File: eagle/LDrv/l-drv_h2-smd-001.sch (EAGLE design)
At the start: 26 parts, among them IC2 74AC132D, IC3 74AC132D, IC4 74AC132D

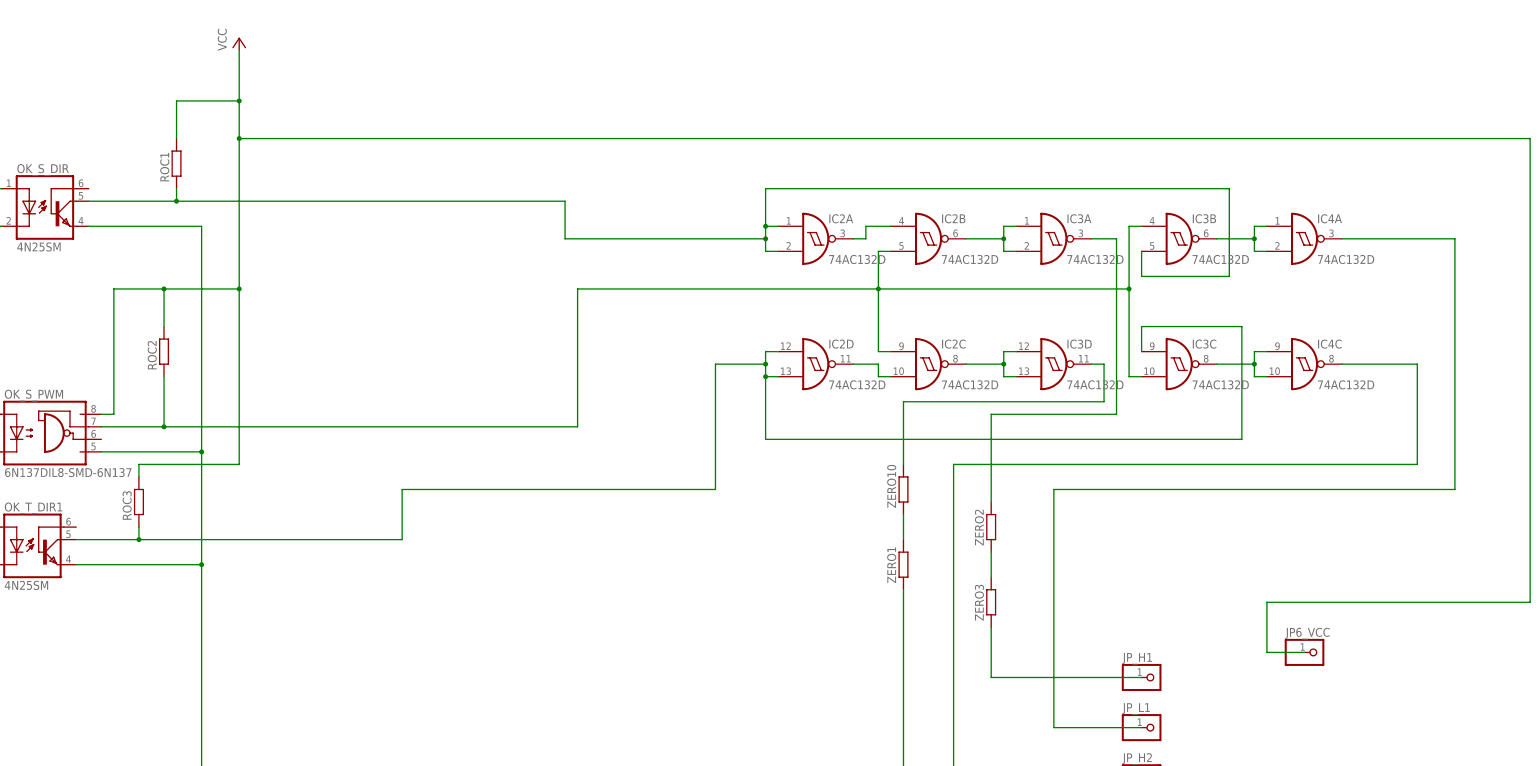
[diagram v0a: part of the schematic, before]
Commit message: SMD logic circit
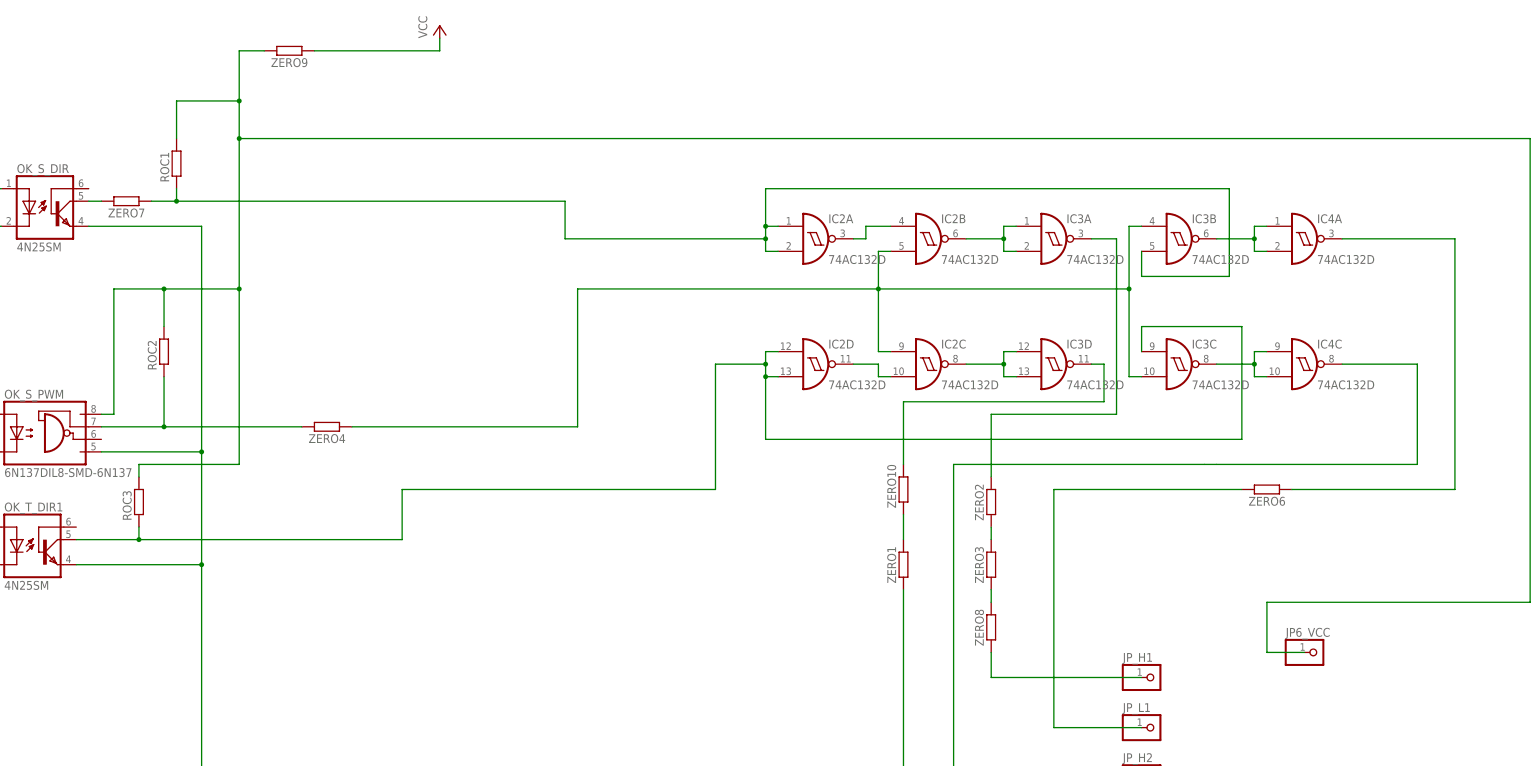
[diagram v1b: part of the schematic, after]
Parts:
- added ZERO4, ZERO6, ZERO7, ZERO8, ZERO9: (no value), rcl:R-EU_R1206
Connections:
- new net N$20: OK_S_PWM.VE, ROC2.1, ZERO4.2
- new net N$23: JP_L1.1, ZERO6.2
- new net N$24: OK_S_DIR.COL, ZERO7.2
- new net N$25: ZERO3.1, ZERO8.2
- new net N$26: JP6_VCC.1, OK_S_PWM.VCC, ROC1.2, ROC2.2, ROC3.2, ZERO9.2
- net N$14: now also ZERO8.1; no longer ZERO3.1
- net N$17: now also ZERO6.1; no longer JP_L1.1
- net N$D1: now also ZERO7.1; no longer OK_S_DIR.COL
- net N$PWM: now also ZERO4.1; no longer OK_S_PWM.VE, ROC2.1
- net VCC: now also ZERO9.1; no longer JP6_VCC.1, OK_S_PWM.VCC, ROC1.2, ROC2.2, ROC3.2
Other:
- moved on the sheet: ZERO2, ZERO3

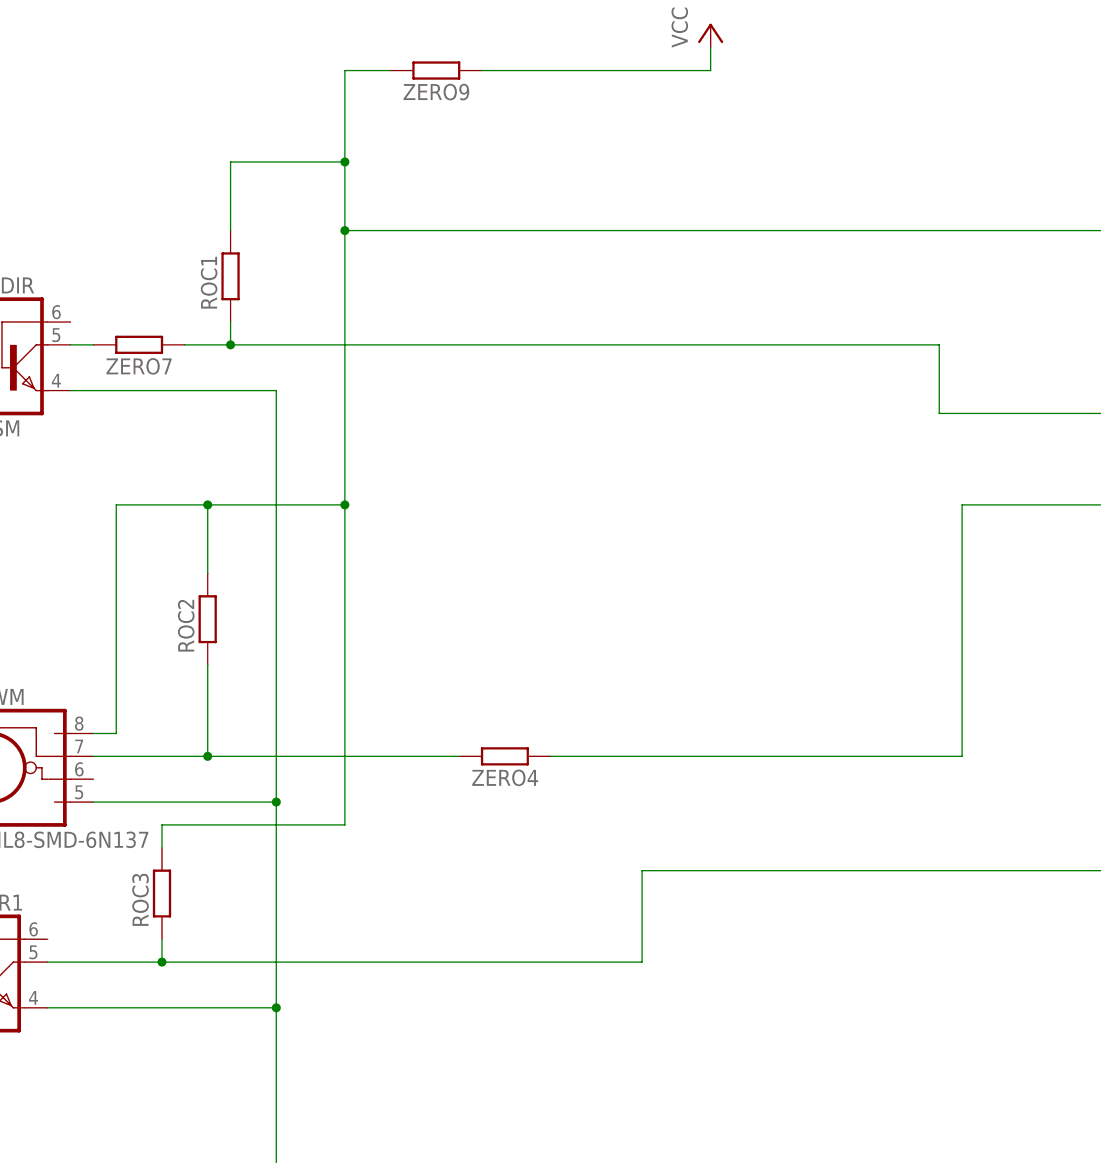
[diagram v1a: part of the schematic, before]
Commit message: SMD for logic drv
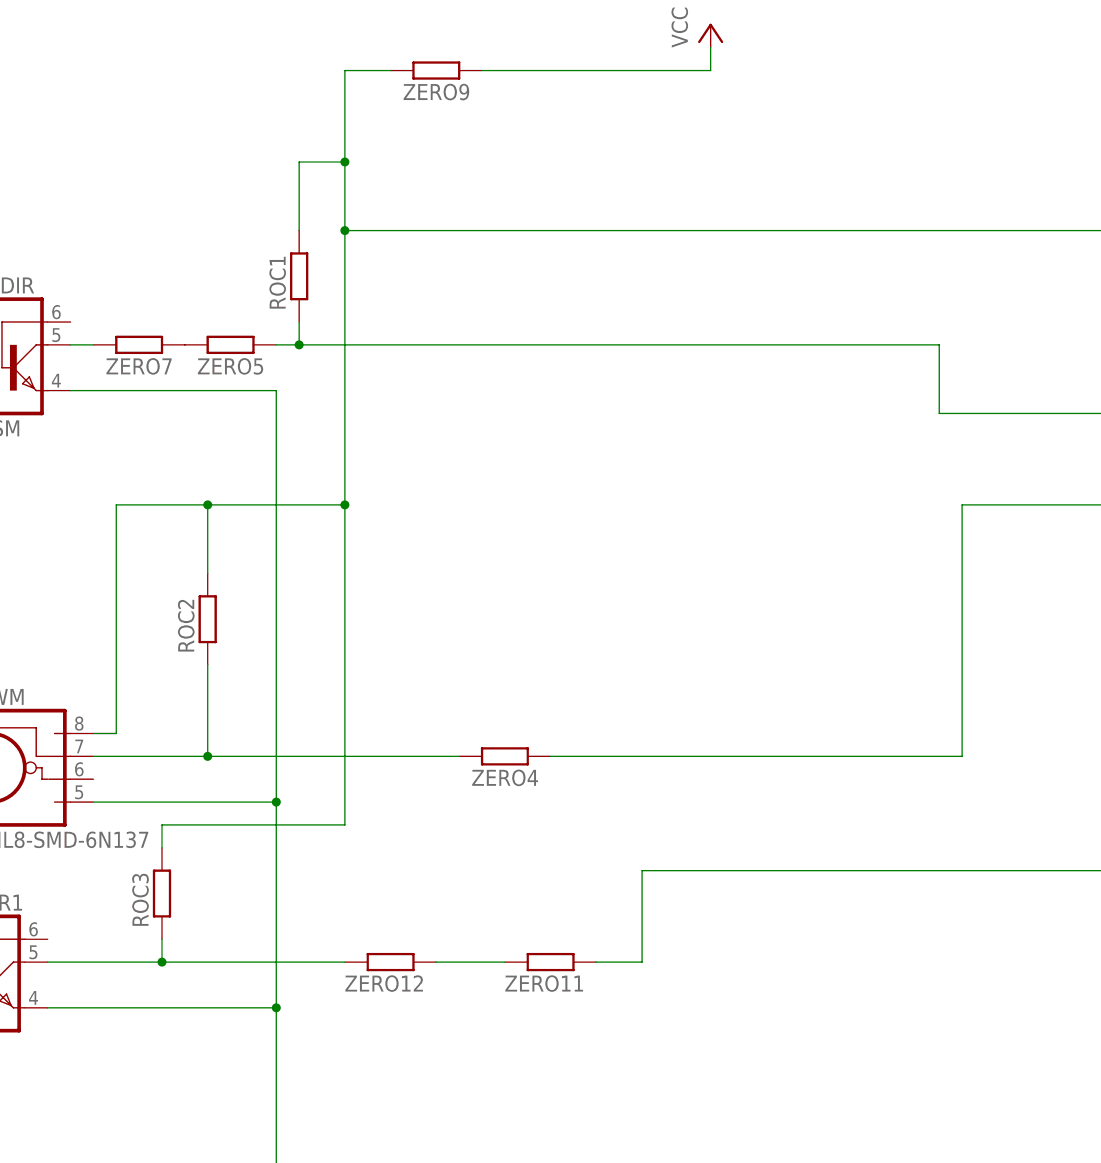
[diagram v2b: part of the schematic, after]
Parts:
- added ZERO11, ZERO12, ZERO5: (no value), rcl:R-EU_R1206
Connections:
- new net N$22: ZERO5.2, ZERO7.1
- new net N$27: OK_T_DIR1.COL, ROC3.1, ZERO12.2
- new net N$28: ZERO11.2, ZERO12.1
- net N$D1: now also ZERO5.1; no longer ZERO7.1
- net N$D2: now also ZERO11.1; no longer OK_T_DIR1.COL, ROC3.1
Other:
- moved on the sheet: ROC1
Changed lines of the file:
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@@
 <setting verticaltext="up"/>
 </settings>
-<grid distance="0.1" unitdist="inch" unit="inch" style="lines" multiple="1" display="yes" altdistance="0.01" altunitdist="inch" altunit="inch"/>
+<grid distance="0.1" unitdist="inch" unit="inch" style="lines" multiple="1" display="no" altdistance="0.01" altunitdist="inch" altunit="inch"/>
 <layers>
 <layer number="1" name="Top" color="4" fill="1" visible="no" active="no"/>
@@
 <part name="ZERO8" library="rcl" deviceset="R-EU_" device="R1206"/>
 <part name="ZERO9" library="rcl" deviceset="R-EU_" device="R1206"/>
+<part name="ZERO5" library="rcl" deviceset="R-EU_" device="R1206"/>
+<part name="ZERO11" library="rcl" deviceset="R-EU_" device="R1206"/>
+<part name="ZERO12" library="rcl" deviceset="R-EU_" device="R1206"/>
 </parts>
 <sheets>
@@
 <instance part="GND1" gate="1" x="83.82" y="-111.76"/>
 <instance part="P+1" gate="VCC" x="132.08" y="93.98"/>
-<instance part="ROC1" gate="G$1" x="78.74" y="66.04" rot="R90"/>
+<instance part="ROC1" gate="G$1" x="86.36" y="66.04" rot="R90"/>
 <instance part="ROC2" gate="G$1" x="76.2" y="27.94" rot="R90"/>
 <instance part="ROC3" gate="G$1" x="71.12" y="-2.54" rot="R90"/>
@@
 <instance part="ZERO8" gate="G$1" x="243.84" y="-27.94" rot="R90"/>
 <instance part="ZERO9" gate="G$1" x="101.6" y="88.9" rot="R180"/>
+<instance part="ZERO5" gate="G$1" x="78.74" y="58.42" rot="R180"/>
+<instance part="ZERO11" gate="G$1" x="114.3" y="-10.16" rot="R180"/>
+<instance part="ZERO12" gate="G$1" x="96.52" y="-10.16" rot="R180"/>
 </instances>
 <busses>
@@
 <net name="N$D2" class="0">
 <segment>
-<pinref part="OK_T_DIR1" gate="G$1" pin="COL"/>
-<wire x1="58.42" y1="-10.16" x2="71.12" y2="-10.16" width="0.1524" layer="91"/>
-<pinref part="ROC3" gate="G$1" pin="1"/>
-<wire x1="71.12" y1="-10.16" x2="71.12" y2="-7.62" width="0.1524" layer="91"/>
-<wire x1="124.46" y1="-10.16" x2="71.12" y2="-10.16" width="0.1524" layer="91"/>
-<junction x="71.12" y="-10.16"/>
+<wire x1="124.46" y1="-10.16" x2="119.38" y2="-10.16" width="0.1524" layer="91"/>
 <wire x1="124.46" y1="-10.16" x2="124.46" y2="0" width="0.1524" layer="91"/>
 <wire x1="124.46" y1="0" x2="187.96" y2="0" width="0.1524" layer="91"/>
@@
 <wire x1="274.32" y1="33.02" x2="274.32" y2="27.94" width="0.1524" layer="91"/>
 <junction x="198.12" y="22.86"/>
+<pinref part="ZERO11" gate="G$1" pin="1"/>
 </segment>
 </net>
@@
 <segment>
 <pinref part="ROC1" gate="G$1" pin="1"/>
-<wire x1="78.74" y1="58.42" x2="78.74" y2="60.96" width="0.1524" layer="91"/>
-<wire x1="73.66" y1="58.42" x2="78.74" y2="58.42" width="0.1524" layer="91"/>
-<wire x1="157.48" y1="58.42" x2="78.74" y2="58.42" width="0.1524" layer="91"/>
-<junction x="78.74" y="58.42"/>
+<wire x1="86.36" y1="58.42" x2="86.36" y2="60.96" width="0.1524" layer="91"/>
+<wire x1="83.82" y1="58.42" x2="86.36" y2="58.42" width="0.1524" layer="91"/>
+<wire x1="157.48" y1="58.42" x2="86.36" y2="58.42" width="0.1524" layer="91"/>
+<junction x="86.36" y="58.42"/>
 <wire x1="157.48" y1="58.42" x2="157.48" y2="50.8" width="0.1524" layer="91"/>
 <wire x1="157.48" y1="50.8" x2="198.12" y2="50.8" width="0.1524" layer="91"/>
@@
 <wire x1="274.32" y1="43.18" x2="274.32" y2="48.26" width="0.1524" layer="91"/>
 <junction x="198.12" y="53.34"/>
-<pinref part="ZERO7" gate="G$1" pin="1"/>
+<pinref part="ZERO5" gate="G$1" pin="1"/>
 </segment>
 </net>
@@
 <wire x1="91.44" y1="71.12" x2="91.44" y2="40.64" width="0.1524" layer="91"/>
 <wire x1="91.44" y1="40.64" x2="91.44" y2="5.08" width="0.1524" layer="91"/>
-<wire x1="78.74" y1="71.12" x2="78.74" y2="78.74" width="0.1524" layer="91"/>
-<wire x1="78.74" y1="78.74" x2="91.44" y2="78.74" width="0.1524" layer="91"/>
+<wire x1="86.36" y1="71.12" x2="86.36" y2="78.74" width="0.1524" layer="91"/>
+<wire x1="86.36" y1="78.74" x2="91.44" y2="78.74" width="0.1524" layer="91"/>
 <pinref part="ROC3" gate="G$1" pin="2"/>
 <wire x1="71.12" y1="2.54" x2="71.12" y2="5.08" width="0.1524" layer="91"/>
@@
 </segment>
 </net>
+<net name="N$22" class="0">
+<segment>
+<pinref part="ZERO7" gate="G$1" pin="1"/>
+<pinref part="ZERO5" gate="G$1" pin="2"/>
+</segment>
+</net>
+<net name="N$27" class="0">
+<segment>
+<pinref part="ROC3" gate="G$1" pin="1"/>
+<wire x1="71.12" y1="-10.16" x2="71.12" y2="-7.62" width="0.1524" layer="91"/>
+<junction x="71.12" y="-10.16"/>
+<pinref part="OK_T_DIR1" gate="G$1" pin="COL"/>
+<wire x1="91.44" y1="-10.16" x2="71.12" y2="-10.16" width="0.1524" layer="91"/>
+<wire x1="58.42" y1="-10.16" x2="71.12" y2="-10.16" width="0.1524" layer="91"/>
+<pinref part="ZERO12" gate="G$1" pin="2"/>
+</segment>
+</net>
+<net name="N$28" class="0">
+<segment>
+<pinref part="ZERO11" gate="G$1" pin="2"/>
+<wire x1="109.22" y1="-10.16" x2="101.6" y2="-10.16" width="0.1524" layer="91"/>
+<pinref part="ZERO12" gate="G$1" pin="1"/>
+</segment>
+</net>
